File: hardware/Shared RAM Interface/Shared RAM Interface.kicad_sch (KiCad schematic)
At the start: 2 parts, among them U1 74HC245, U2 HY6264AxP

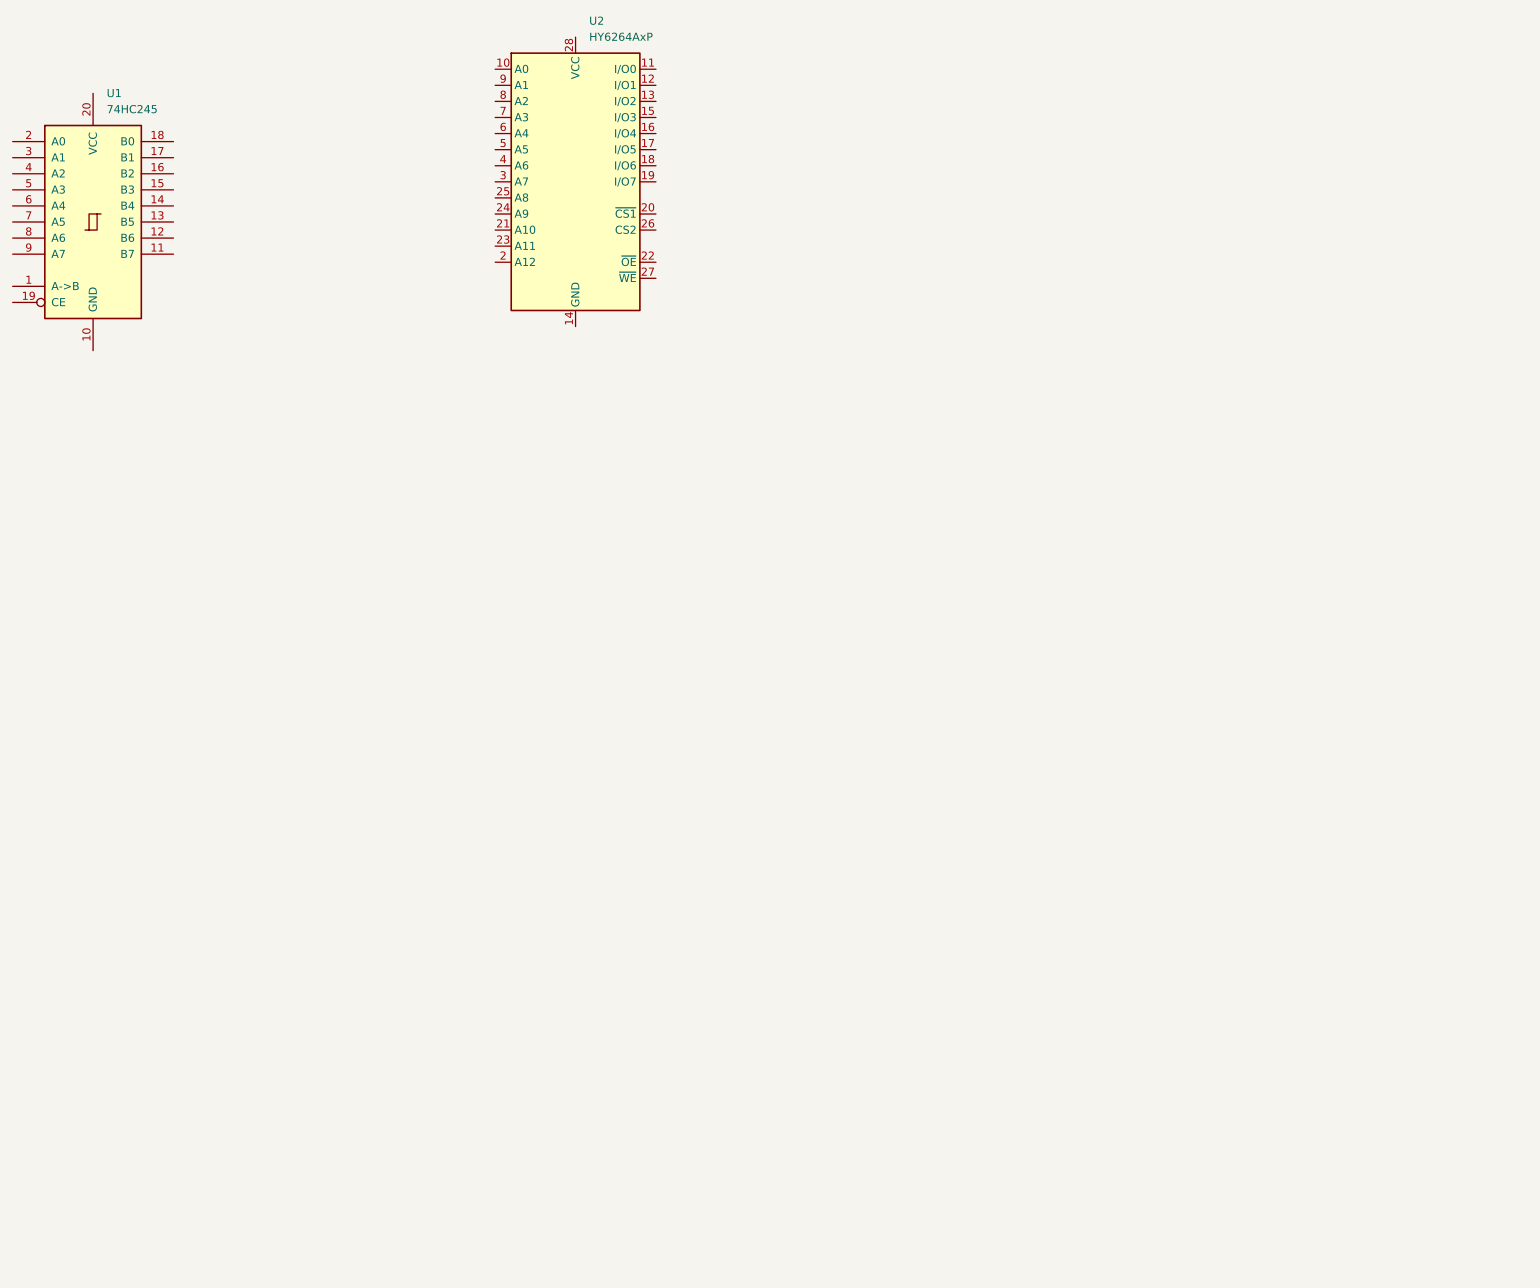
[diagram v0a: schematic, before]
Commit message: updated routing, still needs logic checked
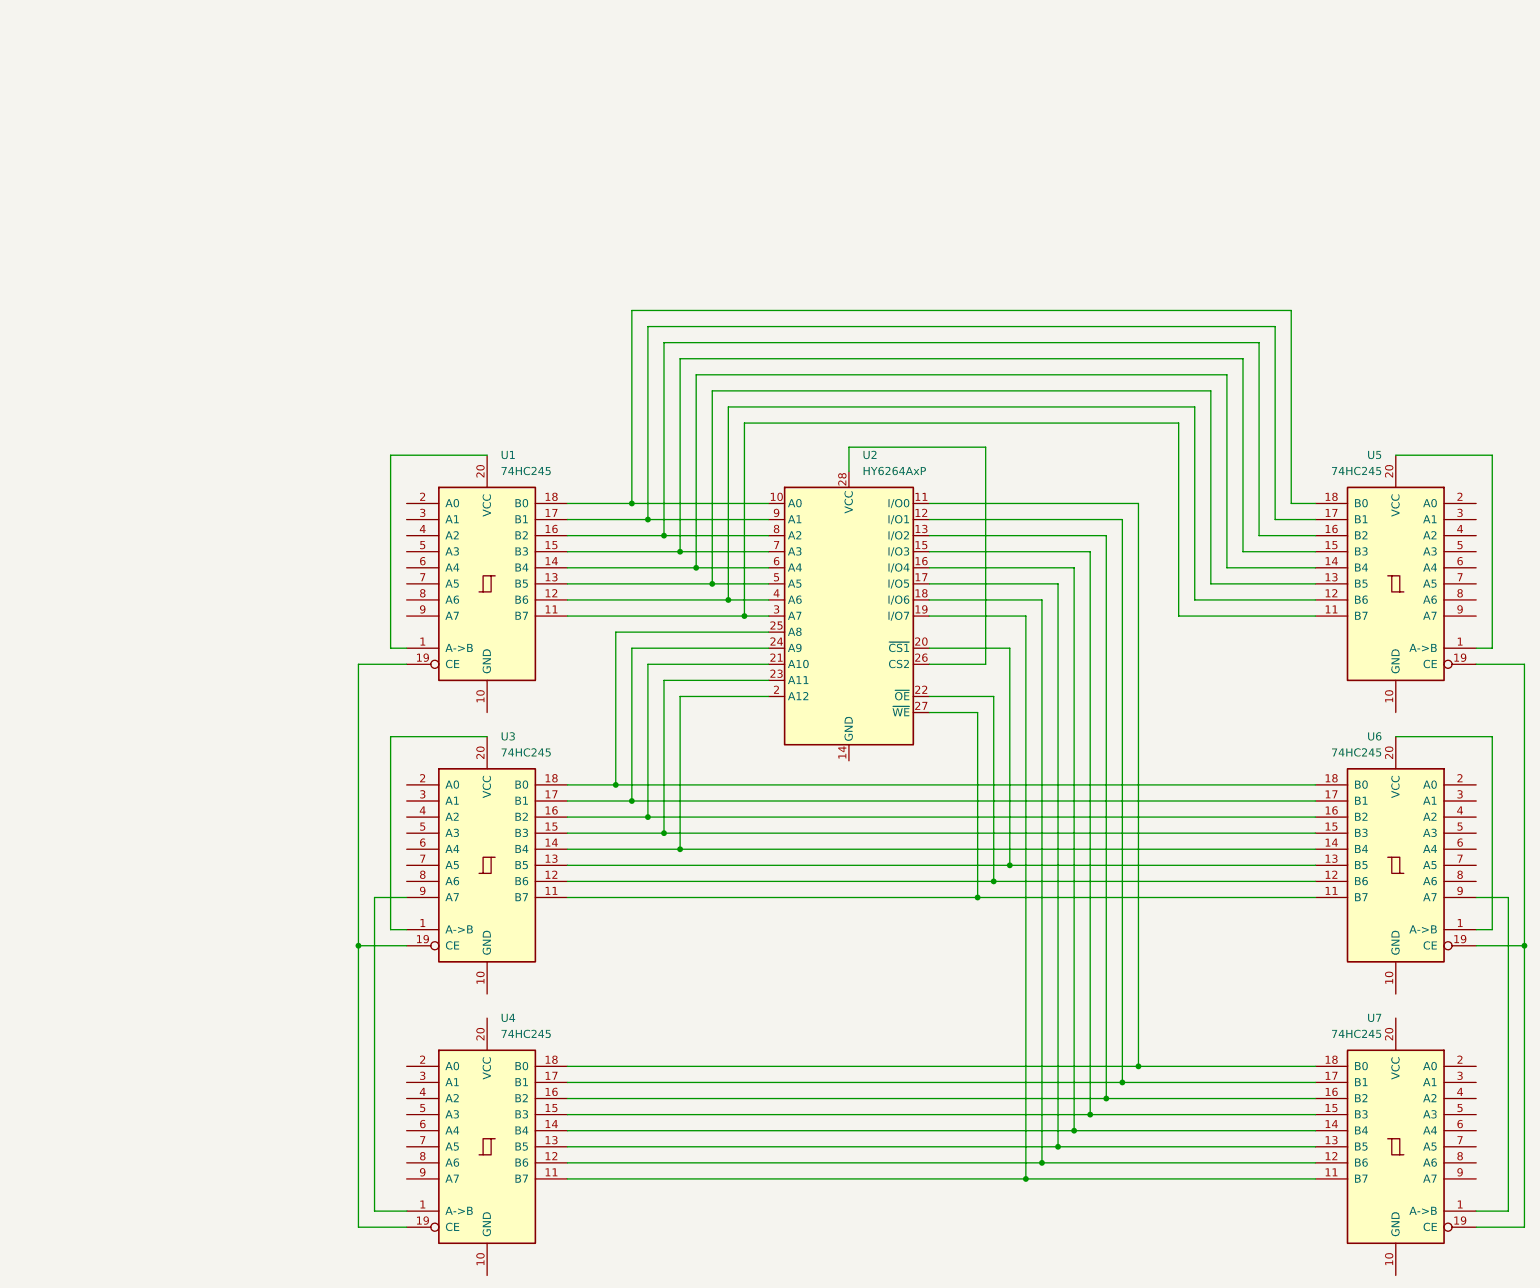
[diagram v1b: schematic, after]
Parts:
- added U3, U4, U5, U6, U7: 74HC245, symbol 74xx:74HC245
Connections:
- net at U2.10 (A0): now also U1.18 (B0), U5.18 (B0)
- net at U2.11 (I/O0): now also U4.18 (B0), U7.18 (B0)
- net at U2.12 (I/O1): now also U4.17 (B1), U7.17 (B1)
- net at U2.13 (I/O2): now also U4.16 (B2), U7.16 (B2)
- net at U2.15 (I/O3): now also U4.15 (B3), U7.15 (B3)
- net at U2.16 (I/O4): now also U4.14 (B4), U7.14 (B4)
- net at U2.17 (I/O5): now also U4.13 (B5), U7.13 (B5)
- net at U2.18 (I/O6): now also U4.12 (B6), U7.12 (B6)
- net at U2.19 (I/O7): now also U4.11 (B7), U7.11 (B7)
- net at U2.2 (A12): now also U3.14 (B4), U6.14 (B4)
- net at U2.20 (~{CS1}): now also U3.13 (B5), U6.13 (B5)
- net at U2.21 (A10): now also U3.16 (B2), U6.16 (B2)
- net at U2.22 (~{OE}): now also U3.12 (B6), U6.12 (B6)
- net at U2.23 (A11): now also U3.15 (B3), U6.15 (B3)
- net at U2.24 (A9): now also U3.17 (B1), U6.17 (B1)
- net at U2.25 (A8): now also U3.18 (B0), U6.18 (B0)
- net at U2.26 (CS2): now also U2.28 (VCC)
- net at U2.27 (~{WE}): now also U3.11 (B7), U6.11 (B7)
- net at U2.3 (A7): now also U1.11 (B7), U5.11 (B7)
- net at U2.4 (A6): now also U1.12 (B6), U5.12 (B6)
- net at U2.5 (A5): now also U1.13 (B5), U5.13 (B5)
- net at U2.6 (A4): now also U1.14 (B4), U5.14 (B4)
- net at U2.7 (A3): now also U1.15 (B3), U5.15 (B3)
- net at U2.8 (A2): now also U1.16 (B2), U5.16 (B2)
- net at U2.9 (A1): now also U1.17 (B1), U5.17 (B1)
- net at U1.1 (A->B): now also U1.20 (VCC)
- net at U1.19 (CE): now also U3.19 (CE), U4.19 (CE)
- new net: U5.1 (A->B), U5.20 (VCC)
- new net: U5.19 (CE), U6.19 (CE), U7.19 (CE)
- new net: U3.1 (A->B), U3.20 (VCC)
- new net: U3.9 (A7), U4.1 (A->B)
- new net: U6.1 (A->B), U6.20 (VCC)
- new net: U6.9 (A7), U7.1 (A->B)
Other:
- moved on the sheet: U1, U2

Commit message: ignore KiCad backup files
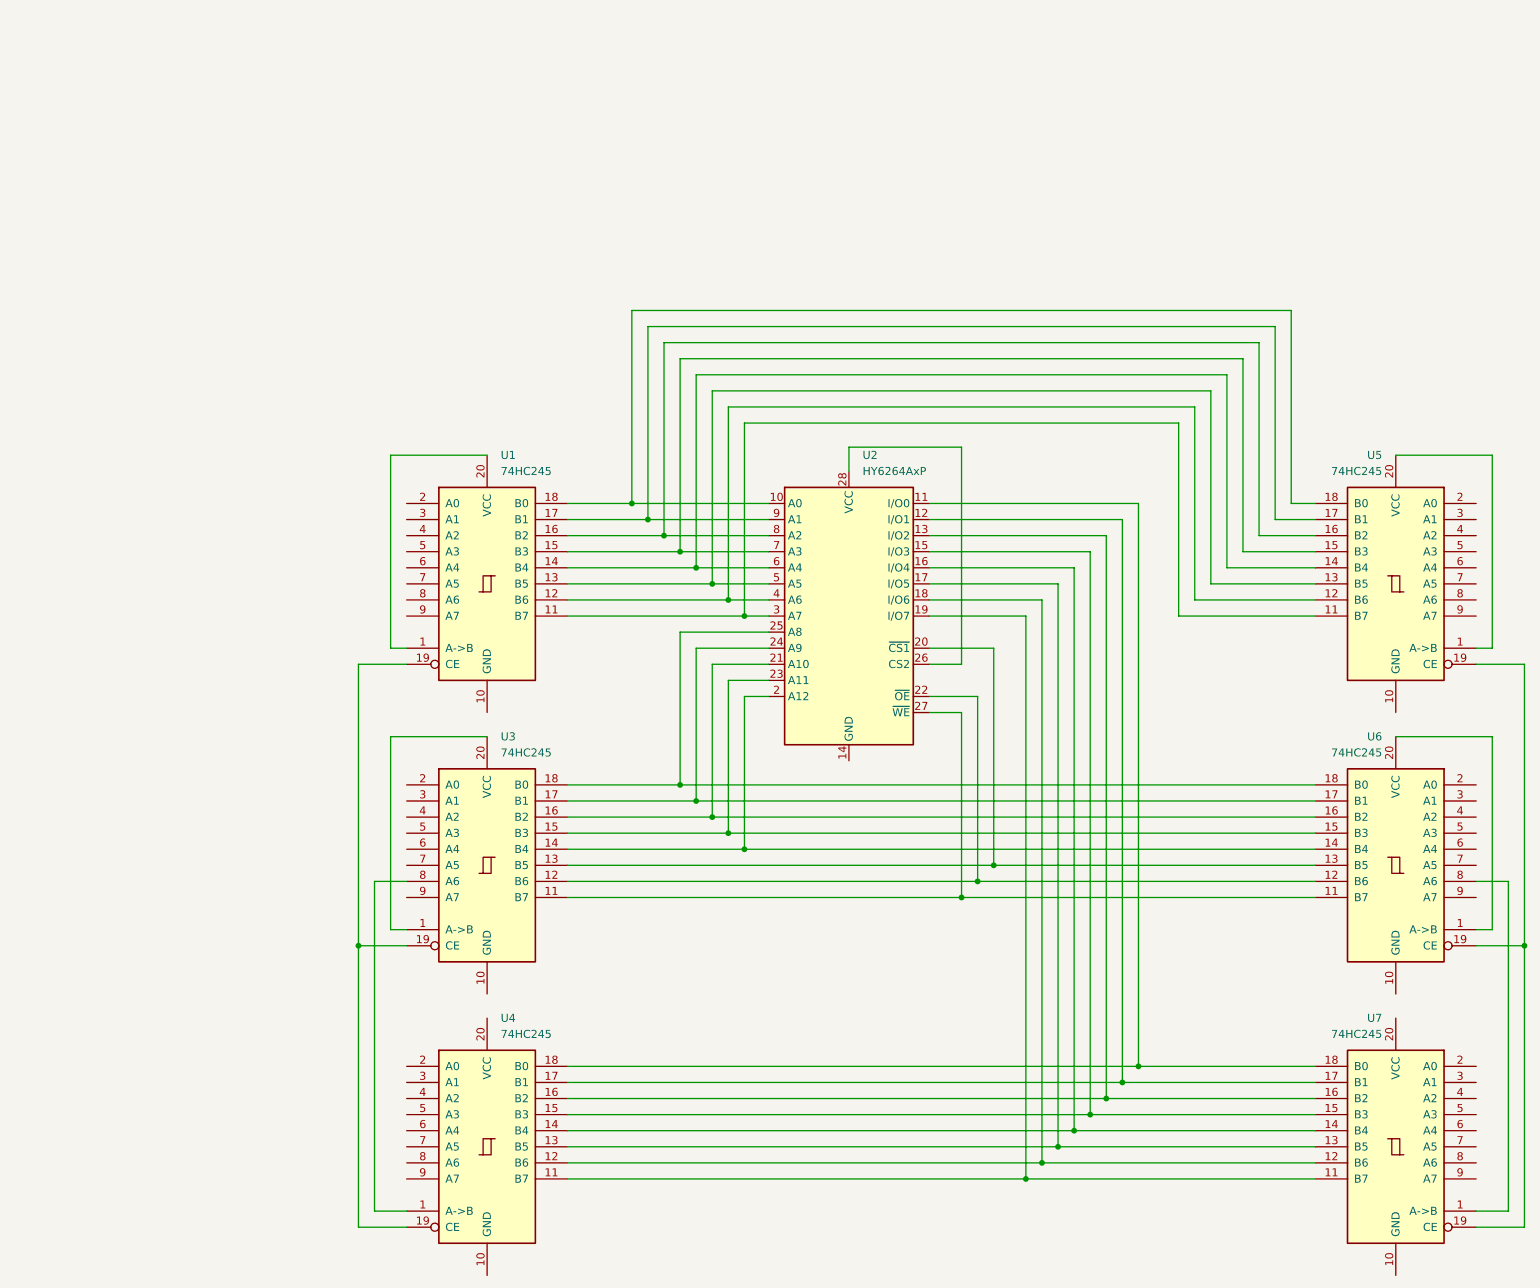
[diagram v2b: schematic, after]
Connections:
- net at U3.8 (A6): now also U4.1 (A->B)
- net at U3.9 (A7): no longer U4.1 (A->B)
- net at U6.8 (A6): now also U7.1 (A->B)
- net at U6.9 (A7): no longer U7.1 (A->B)
